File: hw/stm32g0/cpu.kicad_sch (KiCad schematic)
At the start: 27 parts, among them J201 Conn_01x06, J202 Conn_01x04, J203 Conn_01x03, U201 STM32G030K8Tx, U202 74AHCT125, U203 CAT24C256

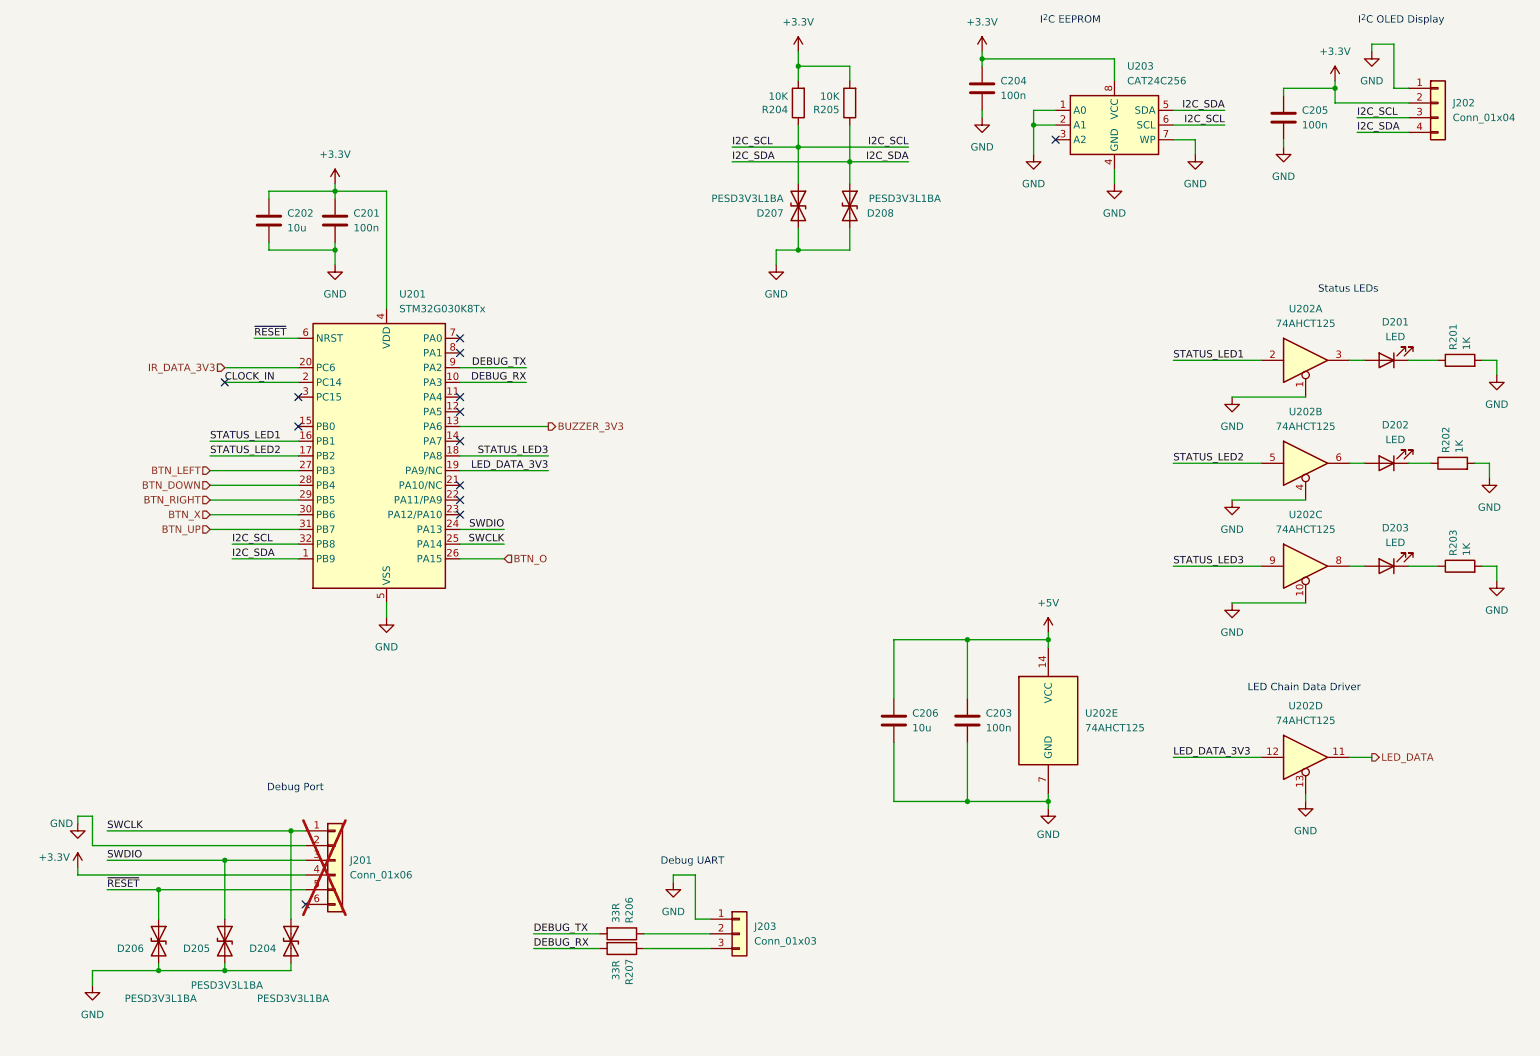
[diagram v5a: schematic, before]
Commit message: chore(hw): add more ESD protection
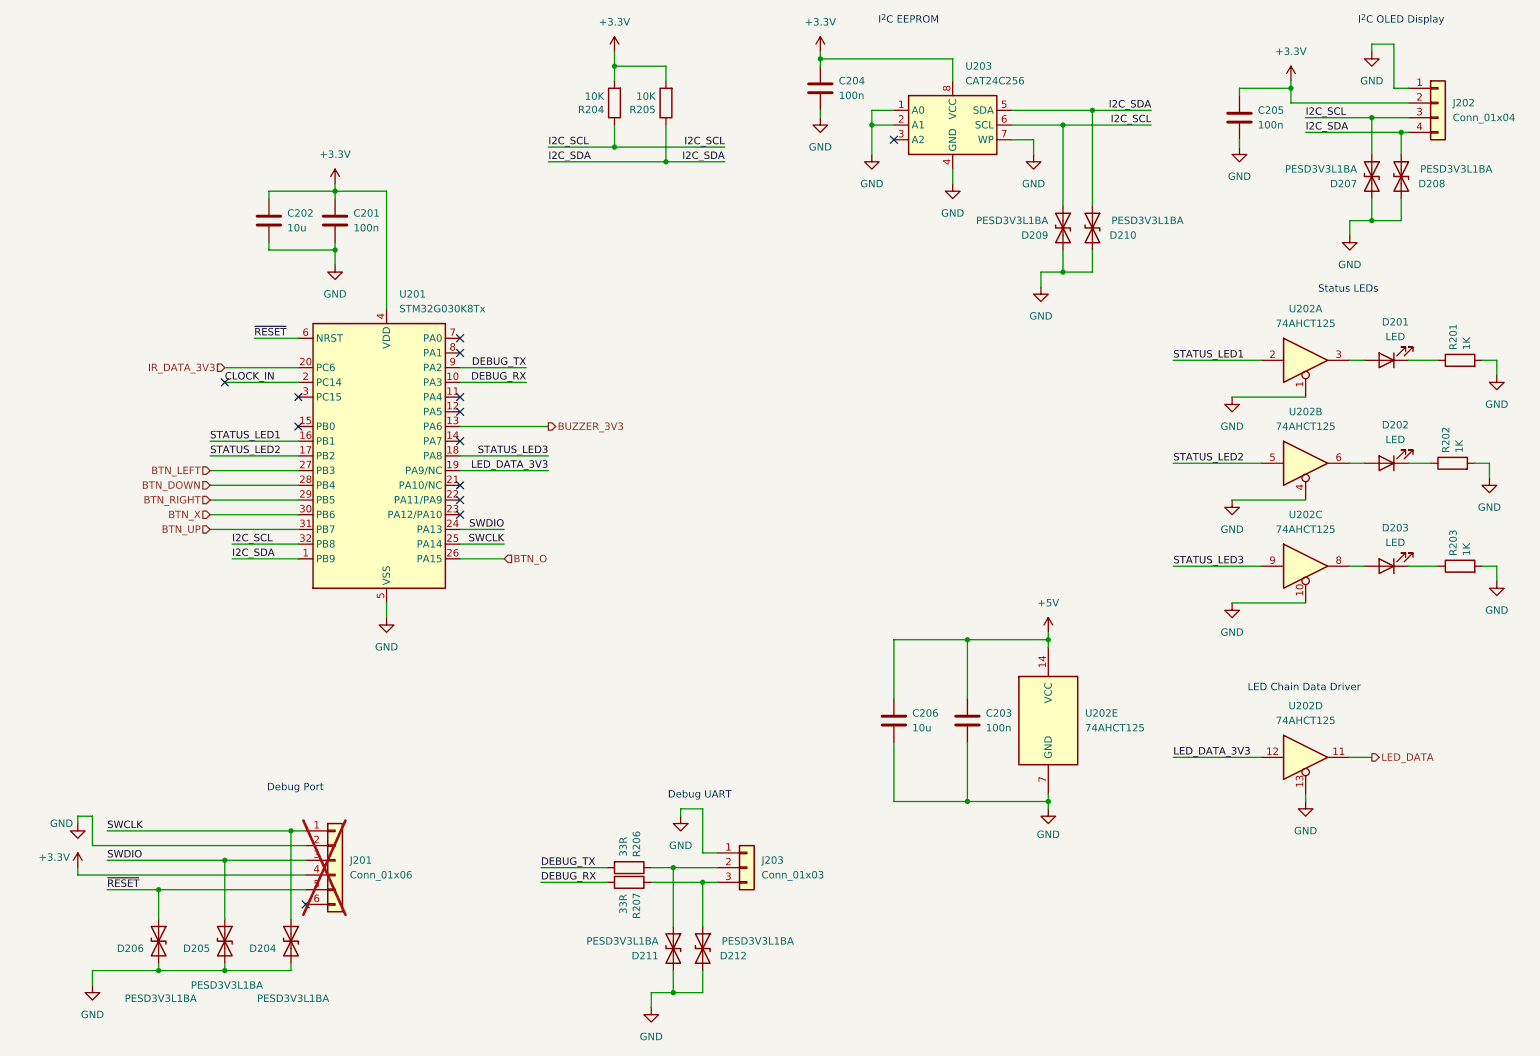
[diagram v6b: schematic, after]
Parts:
- added D209, D210, D211, D212: PESD3V3L1BA, Diode_SMD:D_SOD-323_HandSoldering, symbol Device:D_TVS
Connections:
- net GND: now also D209.2 (A2), D210.2 (A2), D211.2 (A2), D212.2 (A2)
- net I2C_SCL: now also D209.1 (A1)
- net I2C_SDA: now also D210.1 (A1)
- net at J203.3 (Pin_3), R207.1: now also D212.1 (A1)
- net at J203.2 (Pin_2), R206.1: now also D211.1 (A1)
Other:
- moved on the sheet: C204, C205, D207, D208, J203, R204, R205, R206, R207, U203

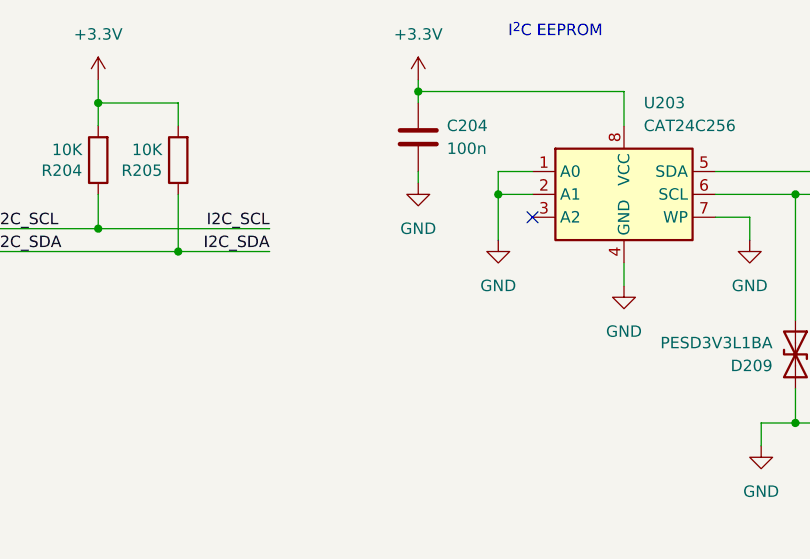
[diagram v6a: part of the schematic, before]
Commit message: chore(hw): add stacked EEPROM footprint
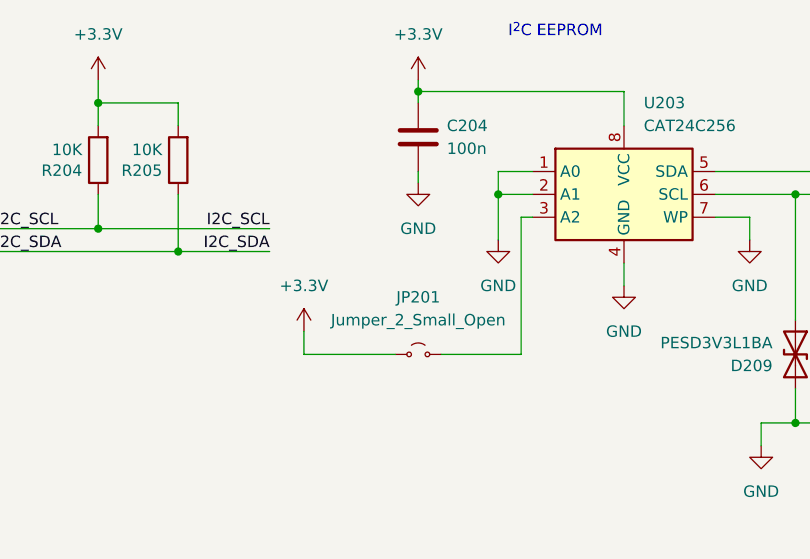
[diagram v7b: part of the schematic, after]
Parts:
- added JP201: Jumper_2_Small_Open, Jumper:SolderJumper-2_P1.3mm_Open_RoundedPad1.0x1.5mm, symbol Jumper:Jumper_2_Small_Open
- U203: footprint Package_DIP:DIP-8_W7.62mm_Socket -> project-specific:DIP-8_W7.62mm_Socket_Stacked_SOIC-8_3.9x4.9mm_P1.27mm
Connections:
- net +3.3V: now also JP201.1 (A)
- net at U203.3 (A2): now also JP201.2 (B)
- no-connect marks 13 -> 12
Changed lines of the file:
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@@
 	)
 	(no_connect
-		(at 172.72 39.37)
-	)
-	(no_connect
 		(at 71.12 171.45)
 	)
@@
 	(wire
 		(pts
+			(xy 147.32 52.07) (xy 147.32 54.61)
+		)
+		(stroke
+			(width 0)
+			(type default)
+		)
+	)
+	(wire
+		(pts
 			(xy 241.3 30.48) (xy 241.3 33.02)
 		)
@@
 	(wire
 		(pts
+			(xy 168.91 36.83) (xy 168.91 41.91)
+		)
+		(stroke
+			(width 0)
+			(type default)
+		)
+	)
+	(wire
+		(pts
 			(xy 133.35 43.18) (xy 143.51 43.18)
 		)
@@
 	(wire
 		(pts
+			(xy 171.45 54.61) (xy 171.45 39.37)
+		)
+		(stroke
+			(width 0)
+			(type default)
+		)
+	)
+	(wire
+		(pts
 			(xy 68.58 158.75) (xy 71.12 158.75)
 		)
@@
 	(wire
 		(pts
+			(xy 162.56 54.61) (xy 171.45 54.61)
+		)
+		(stroke
+			(width 0)
+			(type default)
+		)
+	)
+	(wire
+		(pts
 			(xy 207.01 62.23) (xy 201.93 62.23)
 		)
@@
 	(wire
 		(pts
-			(xy 168.91 41.91) (xy 168.91 36.83)
-		)
-		(stroke
-			(width 0)
-			(type default)
-		)
-	)
-	(wire
-		(pts
 			(xy 172.72 125.73) (xy 185.42 125.73)
 		)
@@
 	(wire
 		(pts
+			(xy 147.32 54.61) (xy 157.48 54.61)
+		)
+		(stroke
+			(width 0)
+			(type default)
+		)
+	)
+	(wire
+		(pts
 			(xy 251.46 113.03) (xy 254 113.03)
 		)
@@
 	(wire
 		(pts
+			(xy 171.45 39.37) (xy 172.72 39.37)
+		)
+		(stroke
+			(width 0)
+			(type default)
+		)
+	)
+	(wire
+		(pts
 			(xy 97.79 78.74) (xy 109.22 78.74)
 		)
@@
 		)
 		(instances
-			(project ""
+			(project "stm32g0"
 				(path "/fc4ba96f-a9f8-4f1a-a9c5-2b16679a6770/32819f2b-3e26-4dff-931e-dc604d389a45"
 					(reference "D204")
@@
 	)
 	(symbol
+		(lib_id "power:+3.3V")
+		(at 147.32 52.07 0)
+		(unit 1)
+		(exclude_from_sim no)
+		(in_bom yes)
+		(on_board yes)
+		(dnp no)
+		(fields_autoplaced yes)
+		(property "Reference" "#PWR0227"
+			(at 147.32 55.88 0)
+			(effects
+				(font
+					(size 1.27 1.27)
+				)
+				(hide yes)
+			)
+		)
+		(property "Value" "+3.3V"
+			(at 147.32 46.99 0)
+			(effects
+				(font
+					(size 1.27 1.27)
+				)
+			)
+		)
+		(property "Footprint" ""
+			(at 147.32 52.07 0)
+			(effects
+				(font
+					(size 1.27 1.27)
+				)
+				(hide yes)
+			)
+		)
+		(property "Datasheet" ""
+			(at 147.32 52.07 0)
+			(effects
+				(font
+					(size 1.27 1.27)
+				)
+				(hide yes)
+			)
+		)
+		(property "Description" "Power symbol creates a global label with name \"+3.3V\""
+			(at 147.32 52.07 0)
+			(effects
+				(font
+					(size 1.27 1.27)
+				)
+				(hide yes)
+			)
+		)
+		(pin "1"
+		)
+		(instances
+			(project "stm32g0"
+				(path "/fc4ba96f-a9f8-4f1a-a9c5-2b16679a6770/32819f2b-3e26-4dff-931e-dc604d389a45"
+					(reference "#PWR0227")
+					(unit 1)
+				)
+			)
+		)
+	)
+	(symbol
 		(lib_id "Memory_EEPROM:CAT24C256")
 		(at 182.88 36.83 0)
@@
 			)
 		)
-		(property "Footprint" "Package_DIP:DIP-8_W7.62mm_Socket"
+		(property "Footprint" "project-specific:DIP-8_W7.62mm_Socket_Stacked_SOIC-8_3.9x4.9mm_P1.27mm"
 			(at 182.88 36.83 0)
 			(effects
@@
 		)
 		(instances
-			(project ""
+			(project "stm32g0"
 				(path "/fc4ba96f-a9f8-4f1a-a9c5-2b16679a6770/32819f2b-3e26-4dff-931e-dc604d389a45"
 					(reference "#PWR0224")
@@
 		)
 		(instances
-			(project ""
+			(project "stm32g0"
 				(path "/fc4ba96f-a9f8-4f1a-a9c5-2b16679a6770/32819f2b-3e26-4dff-931e-dc604d389a45"
 					(reference "#PWR0223")
@@
 					(unit 1)
 				)
+			)
+		)
+	)
+	(symbol
+		(lib_id "Jumper:Jumper_2_Small_Open")
+		(at 160.02 54.61 0)
+		(unit 1)
+		(exclude_from_sim yes)
+		(in_bom yes)
+		(on_board yes)
+		(dnp no)
+		(fields_autoplaced yes)
+		(property "Reference" "JP201"
+			(at 160.02 48.26 0)
+			(effects
+				(font
+					(size 1.27 1.27)
+				)
+			)
+		)
+		(property "Value" "Jumper_2_Small_Open"
+			(at 160.02 50.8 0)
+			(effects
+				(font
+					(size 1.27 1.27)
+				)
+			)
+		)
+		(property "Footprint" "Jumper:SolderJumper-2_P1.3mm_Open_RoundedPad1.0x1.5mm"
+			(at 160.02 54.61 0)
+			(effects
+				(font
+					(size 1.27 1.27)
+				)
+				(hide yes)
+			)
+		)
+		(property "Datasheet" "~"
+			(at 160.02 54.61 0)
+			(effects
+				(font
+					(size 1.27 1.27)
+				)
+				(hide yes)
+			)
+		)
+		(property "Description" "Jumper, 2-pole, small symbol, open"
+			(at 160.02 54.61 0)
+			(effects
+				(font
+					(size 1.27 1.27)
+				)
+				(hide yes)
+			)
+		)
+		(pin "1"
+		)
+		(pin "2"
+		)
+		(instances
+			(project "stm32g0"
+				(path "/fc4ba96f-a9f8-4f1a-a9c5-2b16679a6770/32819f2b-3e26-4dff-931e-dc604d389a45"
+					(reference "JP201")
+					(unit 1)
+				)

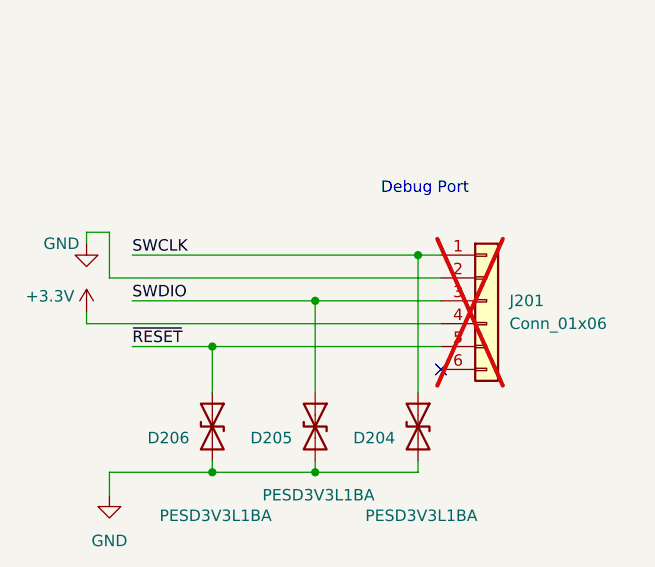
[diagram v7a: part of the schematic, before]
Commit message: chore(hw): update debug stm32g0 debug port pinout
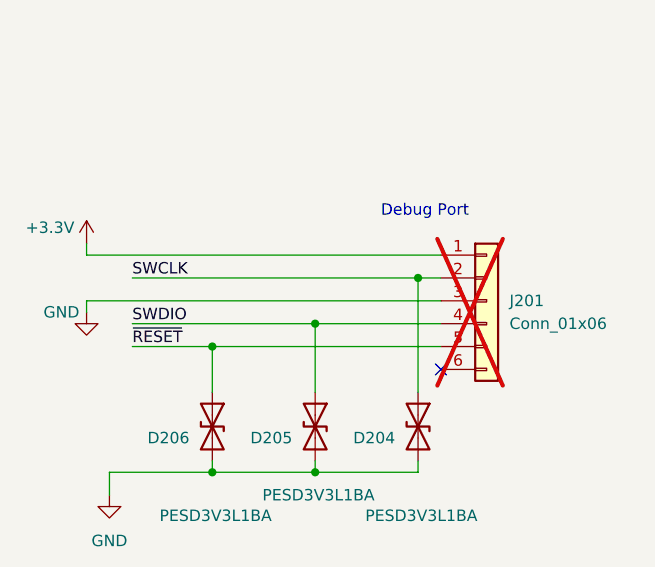
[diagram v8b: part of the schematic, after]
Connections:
- net +3.3V: now also J201.1 (Pin_1); no longer J201.4 (Pin_4)
- net GND: now also J201.3 (Pin_3); no longer J201.2 (Pin_2)
- net SWCLK: now also J201.2 (Pin_2); no longer J201.1 (Pin_1)
- net SWDIO: now also J201.4 (Pin_4); no longer J201.3 (Pin_3)
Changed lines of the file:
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@@
 	)
 	(junction
-		(at 57.15 163.83)
+		(at 57.15 166.37)
 		(diameter 0)
 		(color 0 0 0 0)
@@
 	)
 	(junction
-		(at 68.58 158.75)
+		(at 68.58 161.29)
 		(diameter 0)
 		(color 0 0 0 0)
@@
 	(wire
 		(pts
-			(xy 57.15 163.83) (xy 57.15 173.99)
+			(xy 57.15 166.37) (xy 57.15 173.99)
 		)
 		(stroke
@@
 	(wire
 		(pts
-			(xy 36.83 158.75) (xy 68.58 158.75)
+			(xy 36.83 161.29) (xy 68.58 161.29)
 		)
 		(stroke
@@
 	(wire
 		(pts
-			(xy 31.75 166.37) (xy 71.12 166.37)
+			(xy 31.75 158.75) (xy 71.12 158.75)
 		)
 		(stroke
@@
 	(wire
 		(pts
-			(xy 68.58 158.75) (xy 71.12 158.75)
-		)
-		(stroke
-			(width 0)
-			(type default)
-		)
-	)
-	(wire
-		(pts
-			(xy 34.29 161.29) (xy 71.12 161.29)
+			(xy 68.58 161.29) (xy 71.12 161.29)
 		)
 		(stroke
@@
 	(wire
 		(pts
-			(xy 31.75 165.1) (xy 31.75 166.37)
+			(xy 31.75 157.48) (xy 31.75 158.75)
 		)
 		(stroke
@@
 	(wire
 		(pts
-			(xy 31.75 156.21) (xy 34.29 156.21)
+			(xy 31.75 163.83) (xy 71.12 163.83)
 		)
 		(stroke
@@
 	(wire
 		(pts
-			(xy 57.15 163.83) (xy 71.12 163.83)
+			(xy 57.15 166.37) (xy 71.12 166.37)
 		)
 		(stroke
@@
 	(wire
 		(pts
-			(xy 68.58 158.75) (xy 68.58 173.99)
+			(xy 68.58 161.29) (xy 68.58 173.99)
 		)
 		(stroke
@@
 	(wire
 		(pts
-			(xy 34.29 156.21) (xy 34.29 161.29)
-		)
-		(stroke
-			(width 0)
-			(type default)
-		)
-	)
-	(wire
-		(pts
 			(xy 64.77 48.26) (xy 64.77 49.53)
 		)
@@
 	(wire
 		(pts
-			(xy 31.75 157.48) (xy 31.75 156.21)
+			(xy 31.75 165.1) (xy 31.75 163.83)
 		)
 		(stroke
@@
 	(wire
 		(pts
-			(xy 36.83 163.83) (xy 57.15 163.83)
+			(xy 36.83 166.37) (xy 57.15 166.37)
 		)
 		(stroke
@@
 	(text "Debug Port"
 		(exclude_from_sim no)
-		(at 69.342 151.384 0)
+		(at 69.342 153.924 0)
 		(effects
 			(font
@@
 	)
 	(label "SWCLK"
-		(at 36.83 158.75 0)
+		(at 36.83 161.29 0)
 		(fields_autoplaced yes)
 		(effects
@@
 	)
 	(label "SWDIO"
-		(at 36.83 163.83 0)
+		(at 36.83 166.37 0)
 		(fields_autoplaced yes)
 		(effects
@@
 	(symbol
 		(lib_id "power:+3.3V")
-		(at 31.75 165.1 0)
+		(at 31.75 157.48 0)
 		(unit 1)
 		(exclude_from_sim no)
@@
 		(dnp no)
 		(property "Reference" "#PWR0202"
-			(at 31.75 168.91 0)
+			(at 31.75 161.29 0)
 			(effects
 				(font
@@
 		)
 		(property "Value" "+3.3V"
-			(at 27.686 163.322 0)
+			(at 27.686 155.702 0)
 			(effects
 				(font
@@
 		)
 		(property "Footprint" ""
-			(at 31.75 165.1 0)
+			(at 31.75 157.48 0)
 			(effects
 				(font
@@
 		)
 		(property "Datasheet" ""
-			(at 31.75 165.1 0)
+			(at 31.75 157.48 0)
 			(effects
 				(font
@@
 		)
 		(property "Description" "Power symbol creates a global label with name \"+3.3V\""
-			(at 31.75 165.1 0)
+			(at 31.75 157.48 0)
 			(effects
 				(font
@@
 	(symbol
 		(lib_id "power:GND")
-		(at 31.75 157.48 0)
+		(at 31.75 165.1 0)
 		(unit 1)
 		(exclude_from_sim no)
@@
 		(dnp no)
 		(property "Reference" "#PWR0203"
-			(at 31.75 163.83 0)
+			(at 31.75 171.45 0)
 			(effects
 				(font
@@
 		)
 		(property "Value" "GND"
-			(at 28.956 157.48 0)
+			(at 28.956 165.1 0)
 			(effects
 				(font
@@
 		)
 		(property "Footprint" ""
-			(at 31.75 157.48 0)
+			(at 31.75 165.1 0)
 			(effects
 				(font
@@
 		)
 		(property "Datasheet" ""
-			(at 31.75 157.48 0)
+			(at 31.75 165.1 0)
 			(effects
 				(font
@@
 		)
 		(property "Description" "Power symbol creates a global label with name \"GND\" , ground"
-			(at 31.75 157.48 0)
-			(effects
-				(font
+			(at 31.75 165.1 0)
+			(effects
+				(font
